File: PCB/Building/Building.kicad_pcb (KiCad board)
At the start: 2 copper layers, 61 x 112.1 mm, 34 parts, among them IC1 HT16K33-28SOP, IC2 HT16K33-28SOP, IC3 HT16K33-28SOP, J1 Conn_01x05, U1 OSL60362_IX, U2 OSL60362_IX, U3 OSL60362_IX, U4 OSL60362_IX, U5 OSL60362_IX, U6 OSL60362_IX

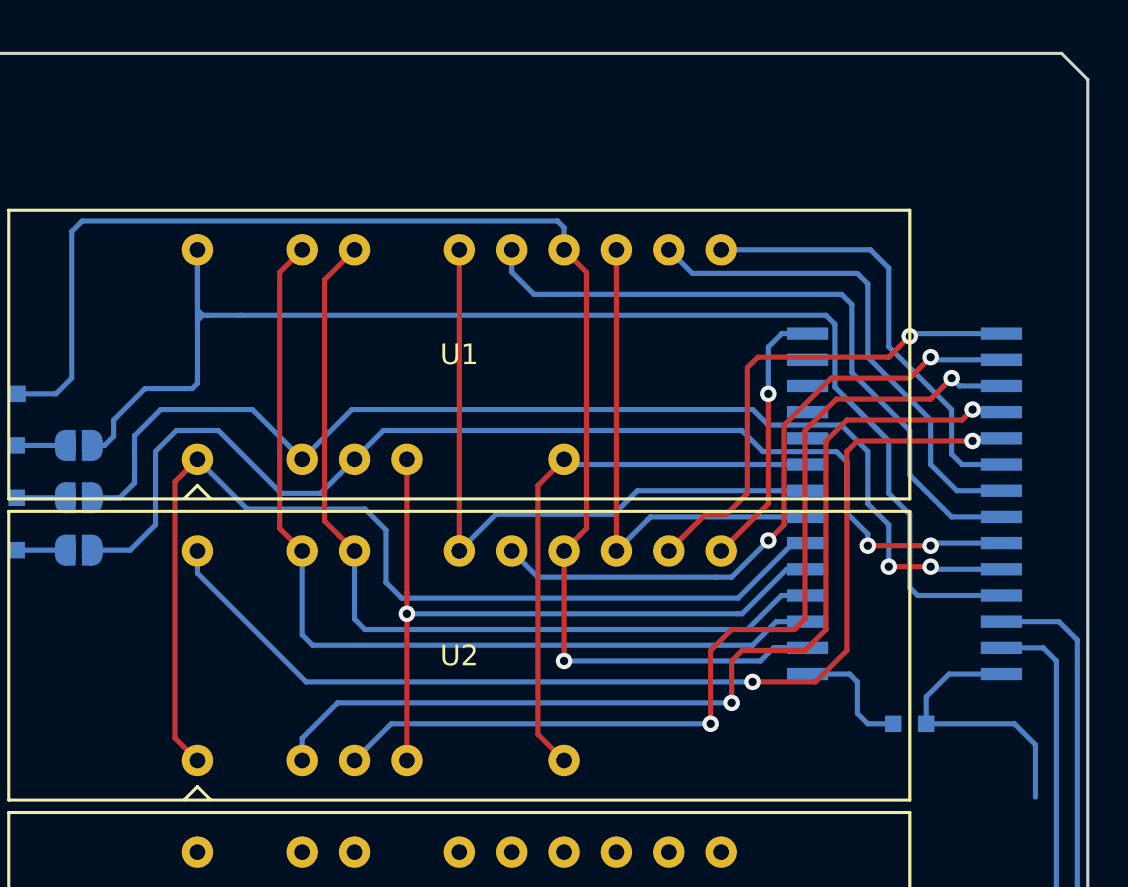
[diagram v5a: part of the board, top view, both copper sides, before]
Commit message: (Building) 配線最適化2 (CA1-6 を上部に束ねるように修正) #75
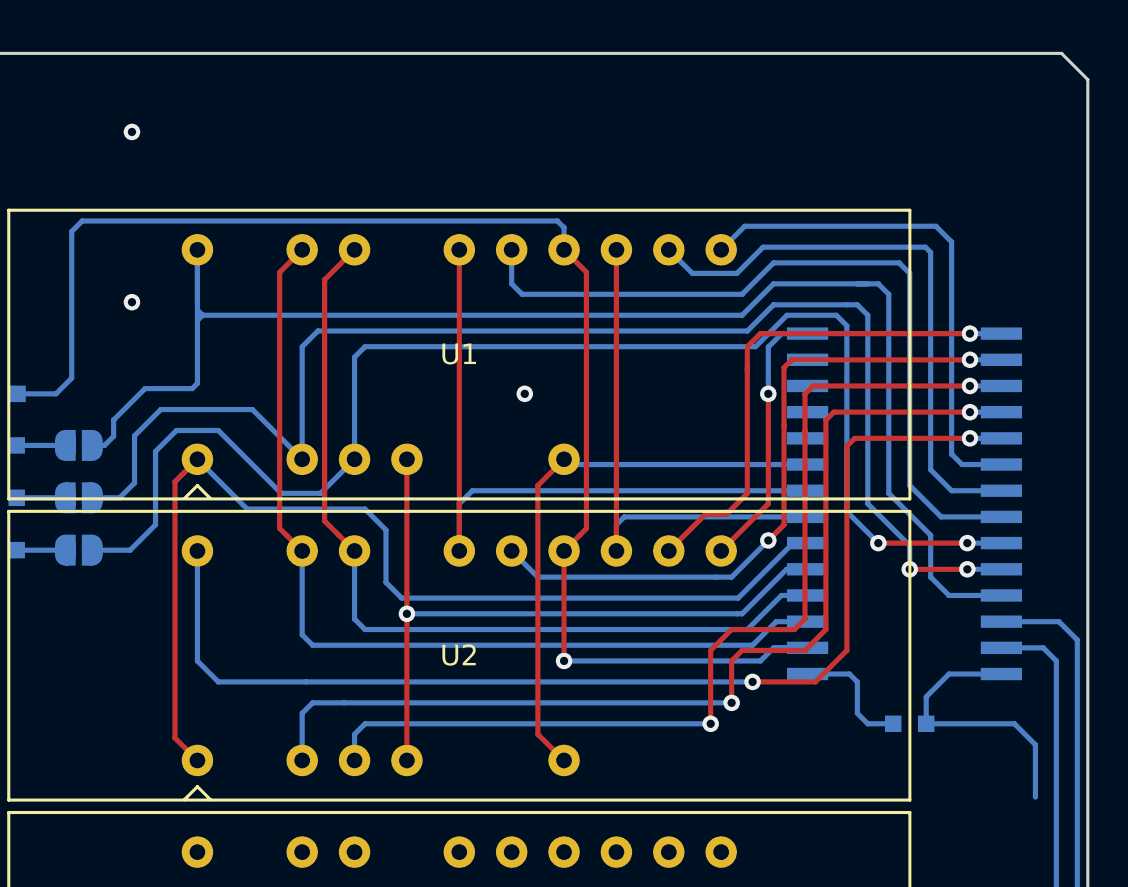
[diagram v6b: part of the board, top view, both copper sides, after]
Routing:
- net /CA3: track 55.3 -> 66.2 mm
- net /CA2: track 55.1 -> 65.8 mm
- net /CA4: track 32.9 -> 37.4 mm
- net /CA5: track 24.3 -> 28.2 mm
- net /CA6: track 21.4 -> 24.9 mm
- net /CA7: track 52.8 -> 55.6 mm
- net /CA10: track 31.6 -> 33.1 mm
- net /CA9: track 46.6 -> 48.1 mm
- net /CA8: track 48.2 -> 49.6 mm
- net /G_1: track 32.7 -> 34.0 mm
- net /CA11: track 24.1 -> 24.9 mm
- net /F_1: track 24.6 -> 25.3 mm
- net GND: vias 1 -> 4

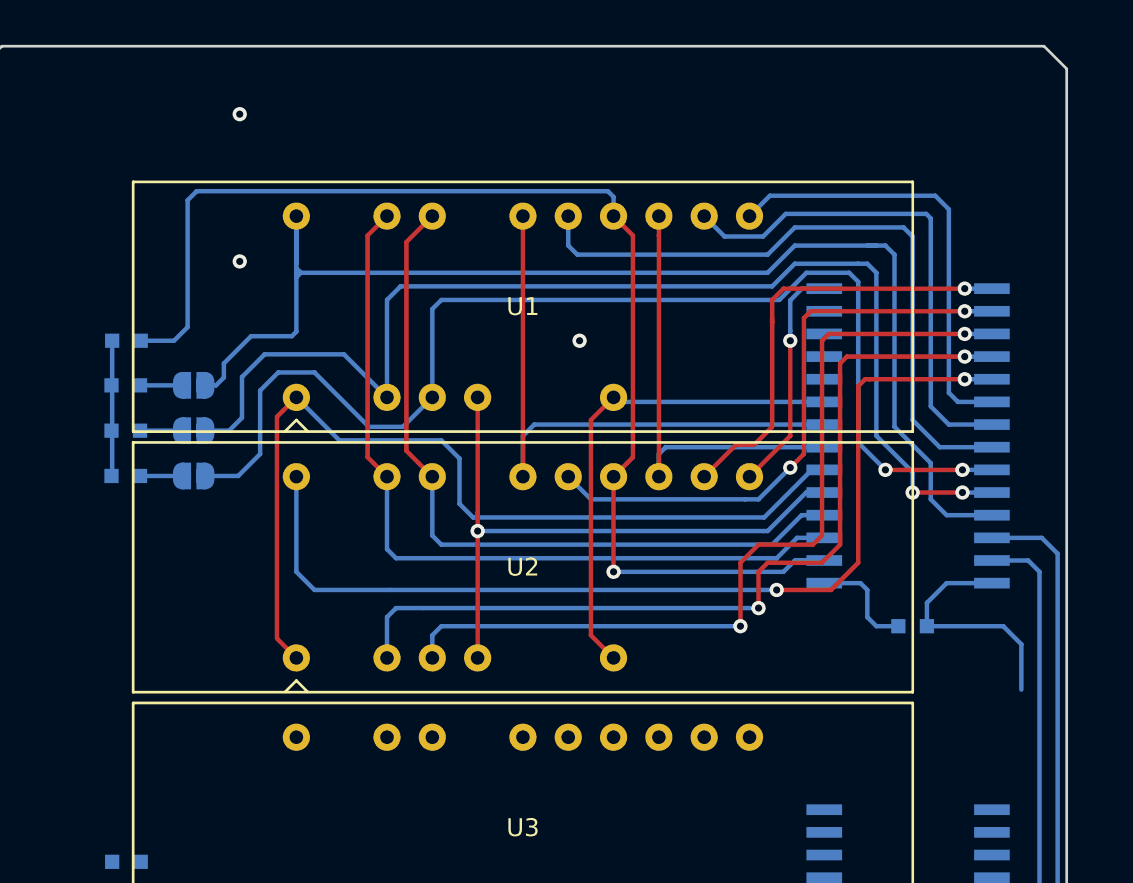
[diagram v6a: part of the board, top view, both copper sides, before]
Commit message: (Building) 配線最適化3 (配線幅を0.5mmに統一) #75
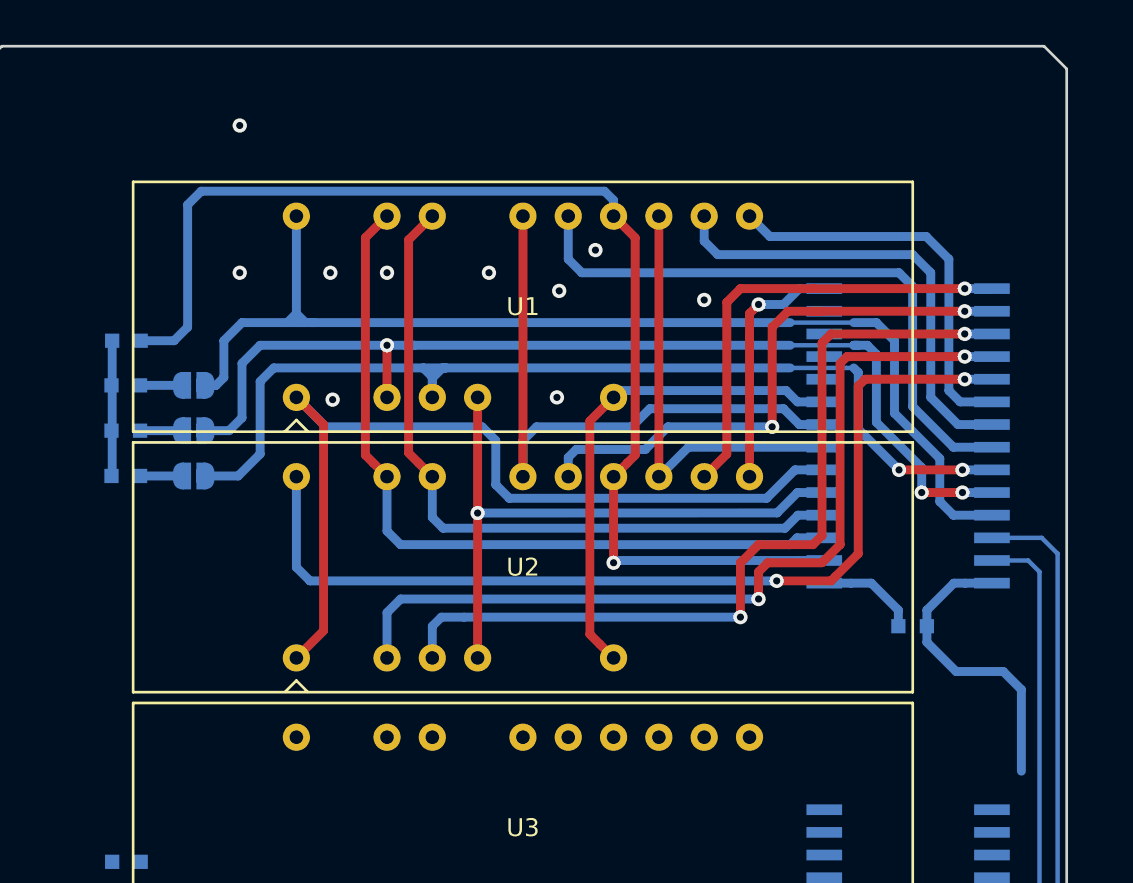
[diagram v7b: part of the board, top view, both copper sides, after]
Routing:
- net /CA3: track 66.2 -> 57.1 mm
- net /CA2: track 65.8 -> 58.0 mm, vias 2 -> 3
- net /CA1: track 69.9 -> 63.5 mm
- net +5V: track 25.5 -> 28.9 mm
- net /CA4: track 37.4 -> 34.5 mm
- net /CA6: track 24.9 -> 22.2 mm
- net /A_1: track 69.8 -> 67.4 mm
- net /CA5: track 28.2 -> 25.9 mm
- net /C_1: track 42.0 -> 40.5 mm
- net /B_1: track 44.8 -> 43.6 mm
- net /CA10: track 33.1 -> 32.1 mm
- net /CA12: track 13.0 -> 13.9 mm
- net /CA7: track 55.6 -> 54.8 mm
- net /F_1: track 25.3 -> 24.6 mm
- net /D_1: track 34.9 -> 35.5 mm
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
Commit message: (Building) 基板外形決定 #75
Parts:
- moved D3 0.51 mm to (116.0, 102.1)
- moved JP8 0.51 mm to (119.8, 107.2)
- moved JP9 0.51 mm to (119.8, 104.6)
- moved R7 0.51 mm to (116.0, 109.7)
- moved R8 0.51 mm to (116.0, 107.2)
- moved R9 0.51 mm to (116.0, 104.6)
- moved JP7 0.51 mm to (119.8, 109.7)
- moved IC3 0.25 mm to (159.7, 107.4)
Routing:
- net SCL: track 125.2 -> 12.5 mm
- net +5V: track 28.9 -> 128.8 mm
- net SDA: track 88.8 -> 14.8 mm
- net GND: vias 11 -> 33
- net /D_1: vias 1 -> 2
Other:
- board size 61 x 112.1 mm -> 57.7 x 111.5 mm
